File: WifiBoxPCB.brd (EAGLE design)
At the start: 65 x 30 mm, 2 parts, among them J1 CONNECTOR_PI_40_PIN, J2 1140084168_1140084168

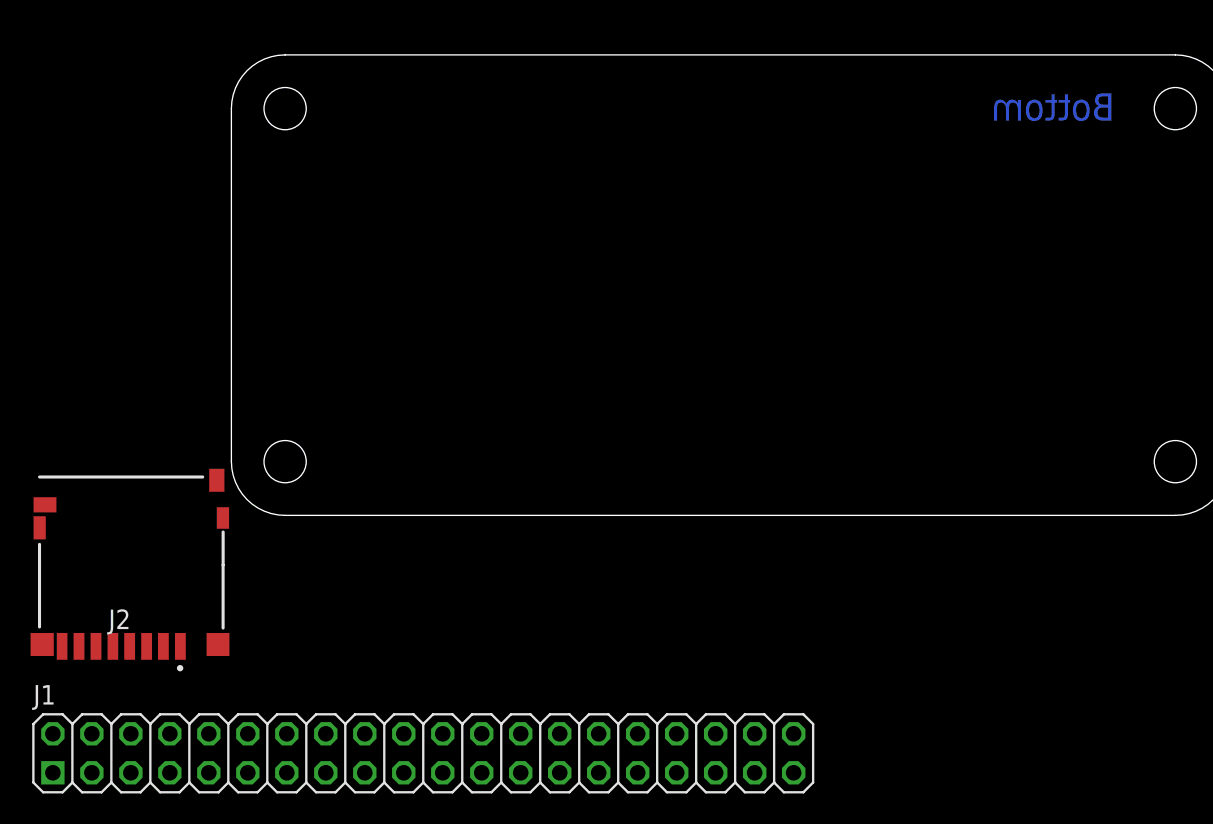
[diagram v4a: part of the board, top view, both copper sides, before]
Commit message: PCB routed contains microSD and OLED screen
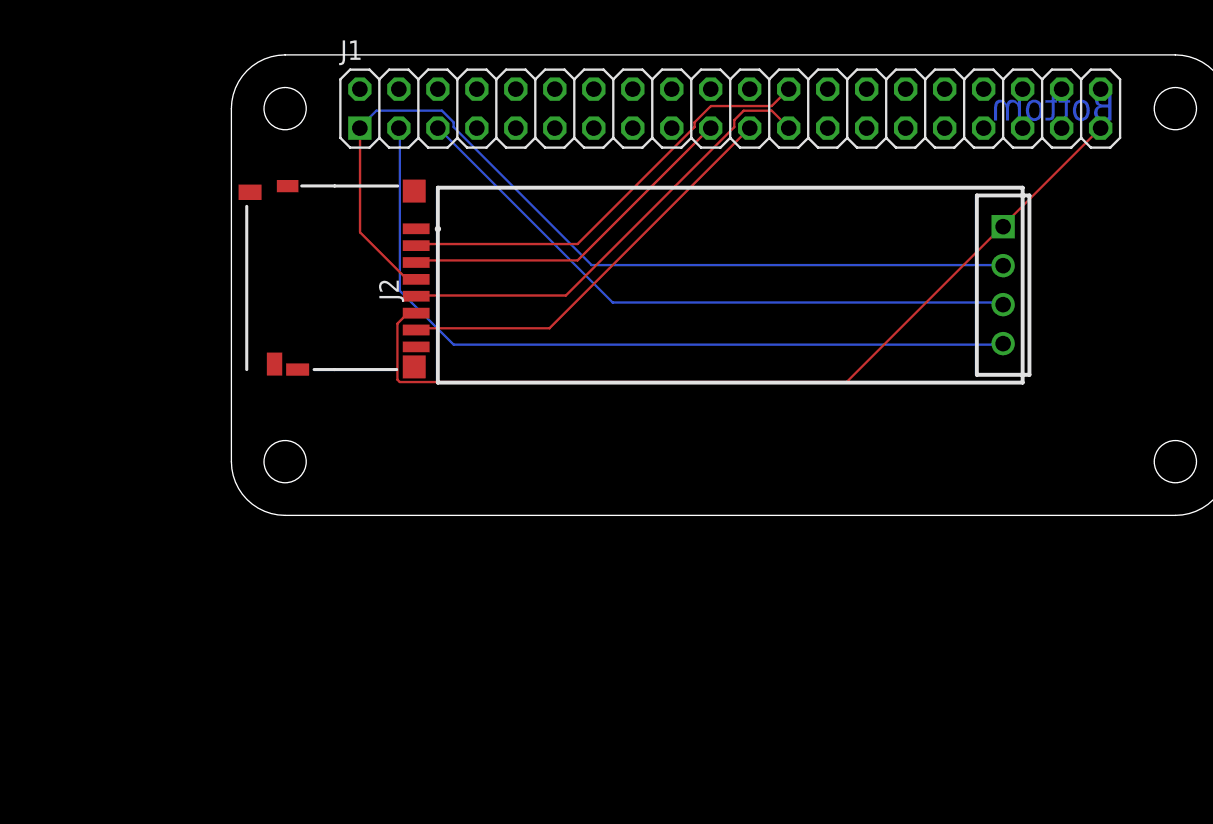
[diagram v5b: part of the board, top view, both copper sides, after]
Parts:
- added J3: CONNECTOR_4, ConnectBox_2019:ESQ-104-XX-X-S
- added U1: OLED_I2C, ConnectBox_2019:OLED-I2C
- moved J1 46.5 mm to (32.5, 26.5)
- moved J2 15.2 mm to (1.00, 9.50), turned to 90 degrees
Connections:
- new net MISO: J1.21, J2.7
- new net SCK: J1.5, J3.3
- new net SCLK: J1.23, J2.5
- new net SDA: J1.3, J3.4
- net +3V3: now also J3.2
- net GND: now also J3.1
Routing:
- net +3V3: track 0.00 -> 58.5 mm
- net GND: track 0.00 -> 57.9 mm
- net SDA: track 0.00 -> 51.4 mm
- net SCK: track 0.00 -> 41.6 mm
- net SCLK: track 0.00 -> 30.1 mm
- net CS: track 0.00 -> 28.7 mm
- net MISO: track 0.00 -> 27.2 mm
- net MOSI: track 0.00 -> 22.9 mm
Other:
- board text added: "APU ConnectBox 2019 2/25/19"

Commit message: update microsd, OLED schematic "value"s.
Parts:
- J2: value 1140084168_1140084168 -> microSD Socket
- J3: value CONNECTOR_4 -> OLED
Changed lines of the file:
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@@
 <?xml version="1.0" encoding="utf-8"?>
 <!DOCTYPE eagle SYSTEM "eagle.dtd">
-<eagle version="9.2.2">
+<eagle version="9.3.1">
 <drawing>
 <settings>
@@
 </autorouter>
 <elements>
-<element name="J2" library="ConnectBox_2019" package="1140084168_1140084168" value="1140084168_1140084168" x="1" y="9.5" smashed="yes" rot="R90">
+<element name="J2" library="ConnectBox_2019" package="1140084168_1140084168" value="microSD Socket" x="1" y="9.5" smashed="yes" rot="R90">
 <attribute name="AVAILABILITY" value="Unavailable" x="1" y="9.5" size="1.778" layer="27" rot="R90" display="off"/>
 <attribute name="DESCRIPTION" value=" Conn; IC Socket; Micro SD; Right Angle; PCB Mount; MicroSD Ser. " x="1" y="9.5" size="1.778" layer="27" rot="R90" display="off"/>
@@
 <attribute name="NAME" x="32.5" y="15" size="2.54" layer="51" ratio="10" rot="R270" align="center"/>
 </element>
-<element name="J3" library="ConnectBox_2019" package="ESQ-104-XX-X-S" value="CONNECTOR_4" x="50.28" y="15" smashed="yes" rot="R270">
+<element name="J3" library="ConnectBox_2019" package="ESQ-104-XX-X-S" value="OLED" x="50.28" y="15" smashed="yes" rot="R270">
 <attribute name="NAME" x="53.455" y="15" size="1.524" layer="25" font="vector" ratio="10" rot="R270" align="center"/>
 <attribute name="NAME" x="50.28" y="15" size="1.524" layer="51" ratio="10" rot="R270" align="center"/>

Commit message: attempting to push items by firts adding them
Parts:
- moved J2 51.5 mm to (52.5, 9.50)
- moved J3 40.5 mm to (9.78, 14.5), turned to 90 degrees
- moved U1 5.02 mm to (27.5, 14.5), turned to 0 degrees
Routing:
- net SDA: track 51.4 -> 7.39 mm
- net SCK: track 41.6 -> 11.0 mm
- net +3V3: track 58.5 -> 73.7 mm, vias 0 -> 1
- net MOSI: track 22.9 -> 37.1 mm
- net GND: track 57.9 -> 68.3 mm, vias 0 -> 1
- net MISO: track 27.2 -> 35.2 mm
- net CS: track 28.7 -> 31.7 mm
- net SCLK: track 30.1 -> 31.8 mm
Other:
- board text added: "APU ConnectBox 2019 3/11/19"
- board text added: "Top"
- board text removed: "APU ConnectBox 2019 2/25/19"

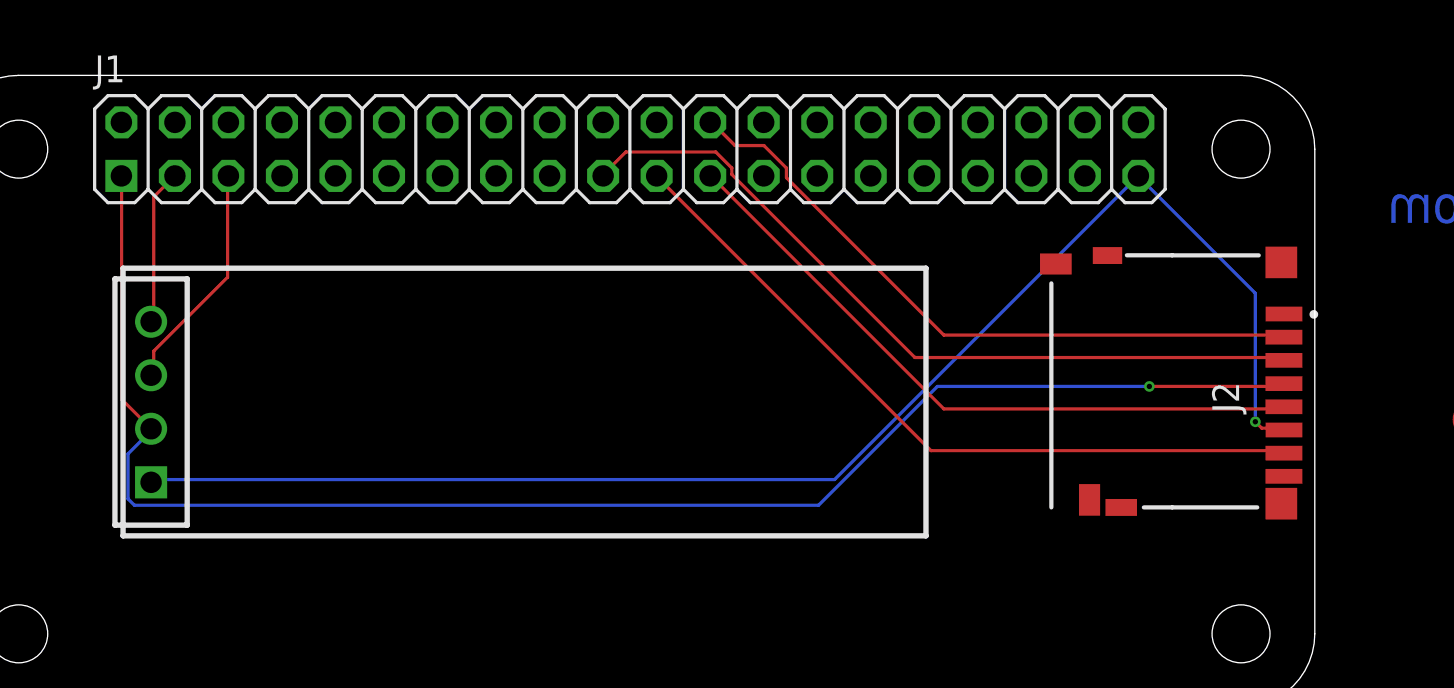
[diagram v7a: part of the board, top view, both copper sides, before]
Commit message: updated rotation on the LED  also replaced SSD card socket to a push push holder
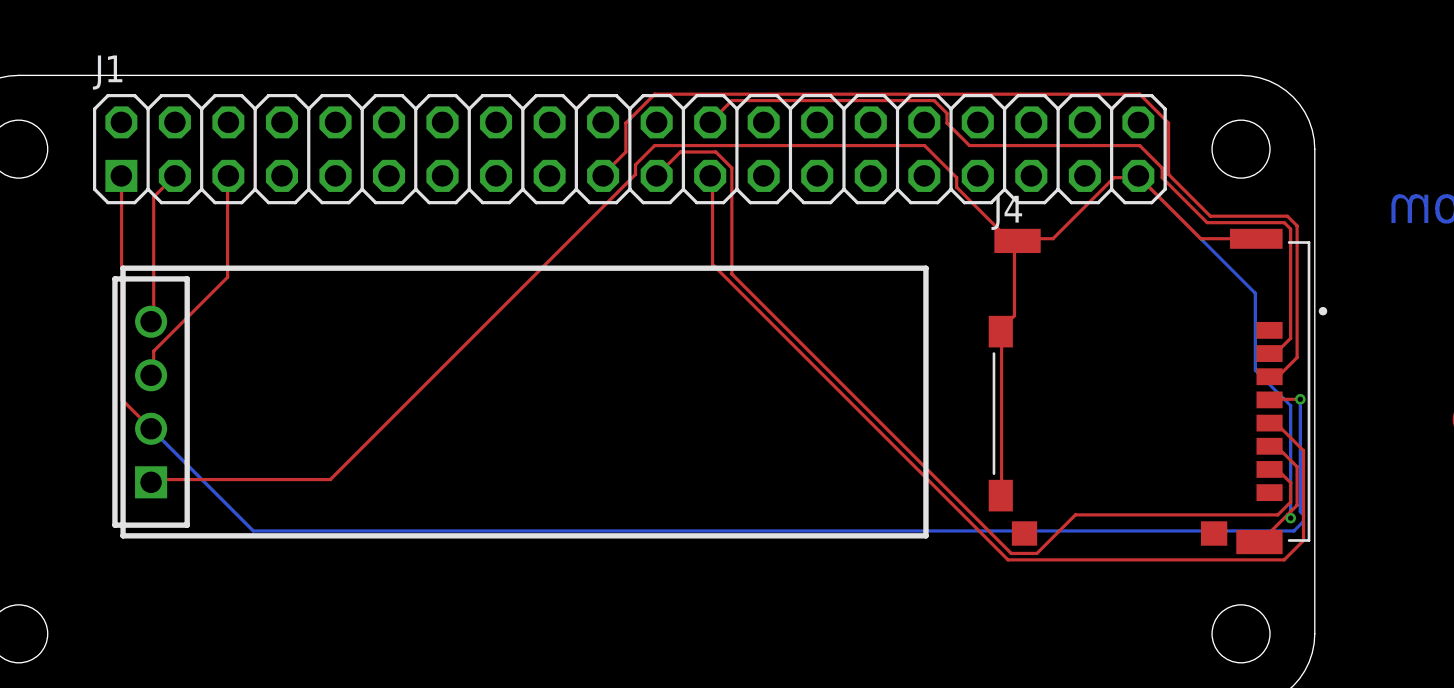
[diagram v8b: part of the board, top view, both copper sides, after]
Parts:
- removed J2: microSD Socket, ConnectBox_2019:1140084168_1140084168
- added J4: 503182-1852, ConnectBox_2019:MOLEX_503182-1852
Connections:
- net +3V3: now also J4.4; no longer J2.4
- net CS: now also J4.2; no longer J2.2
- net GND: now also J4.6, J4.P1, J4.P2, J4.P3, J4.P4, J4.P5; no longer J2.6
- net MISO: now also J4.7; no longer J2.7
- net MOSI: now also J4.3; no longer J2.3
- net SCLK: now also J4.5; no longer J2.5
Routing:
- net GND: track 68.3 -> 102.2 mm
- net SCLK: track 31.8 -> 44.9 mm
- net MOSI: track 37.1 -> 47.3 mm
- net MISO: track 35.2 -> 44.6 mm
- net CS: track 31.7 -> 37.5 mm
- net +3V3: track 73.7 -> 76.8 mm
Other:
- board text added: "APU ConnectBox 2019 3/18/19"
- board text removed: "APU ConnectBox 2019 3/11/19"
